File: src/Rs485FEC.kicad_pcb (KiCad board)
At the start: 2 copper layers, 24 x 27.9 mm, 21 parts, among them J1 B4B-XH-A, P1 105444-0001, Q1 DMP3099L-13, U1 FT232RL, U2 SP485E

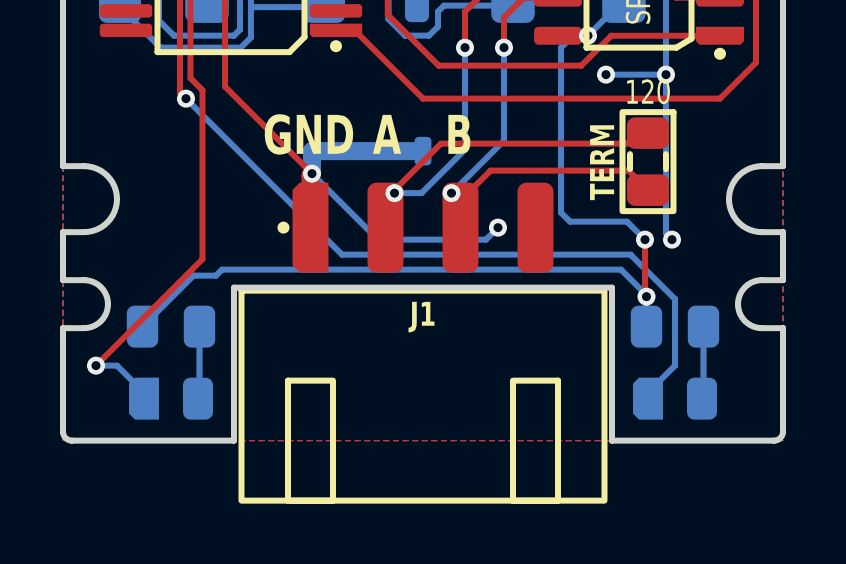
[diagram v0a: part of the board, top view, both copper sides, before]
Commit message: Updated connector designators
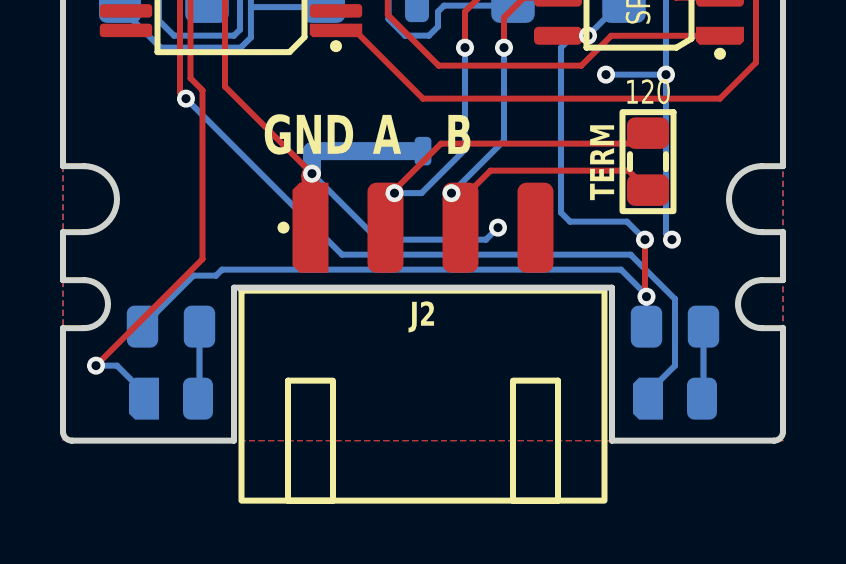
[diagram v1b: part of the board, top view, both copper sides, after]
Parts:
- renumbered P1 to J1, J1 to J2
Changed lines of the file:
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@@
     (descr "Molex 1054440001")
     (attr smd)
-    (fp_text reference "P1" (at 0 -1.7) (layer "F.SilkS") hide
+    (fp_text reference "J1" (at 0 -1.7) (layer "F.SilkS") hide
         (effects (font (size 0.8 0.6) (thickness 0.15)))
     )
@@
     (descr "JST B4B-XH-A [455-B4B-XH-A-ND]")
     (attr through_hole)
-    (fp_text reference "J1" (at 0 2.9) (layer "F.SilkS")
+    (fp_text reference "J2" (at 0 2.9) (layer "F.SilkS")
         (effects (font (size 0.8 0.6) (thickness 0.15) bold))
     )

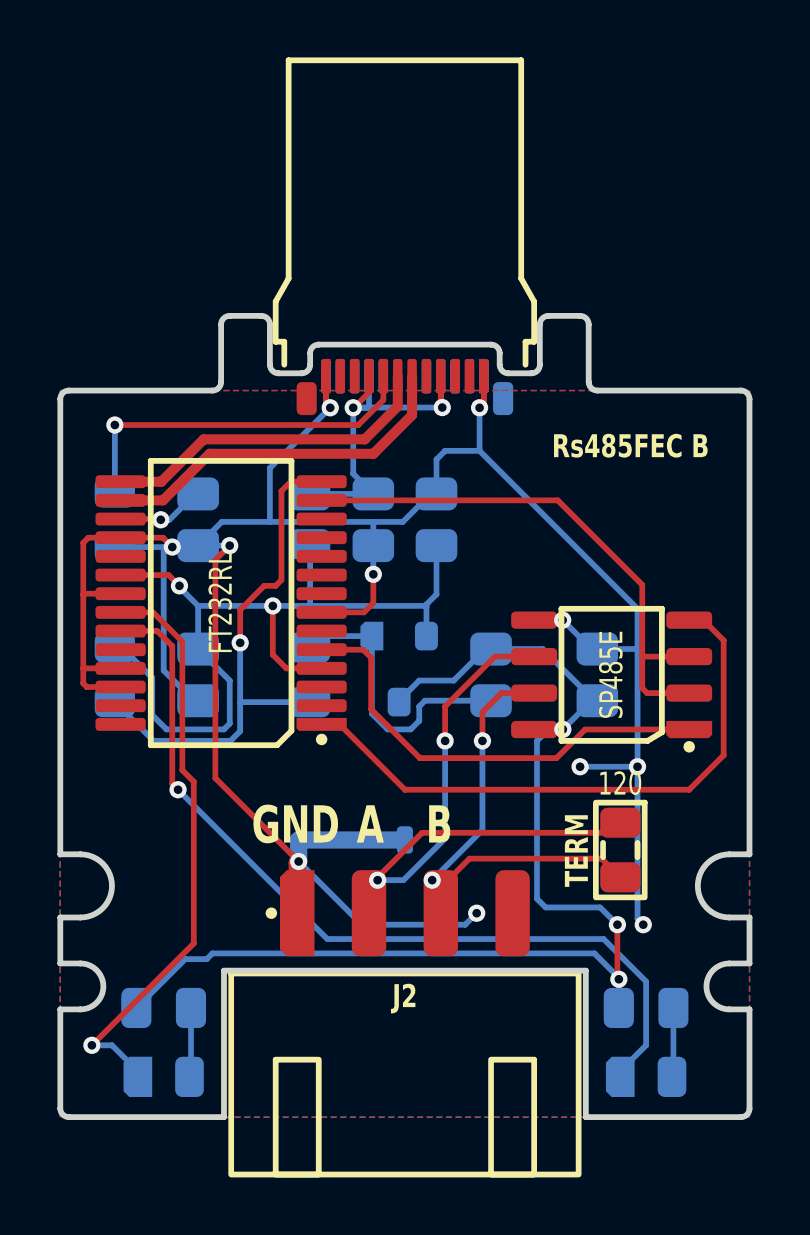
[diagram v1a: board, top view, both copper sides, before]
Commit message: Updated for KiCAD 8
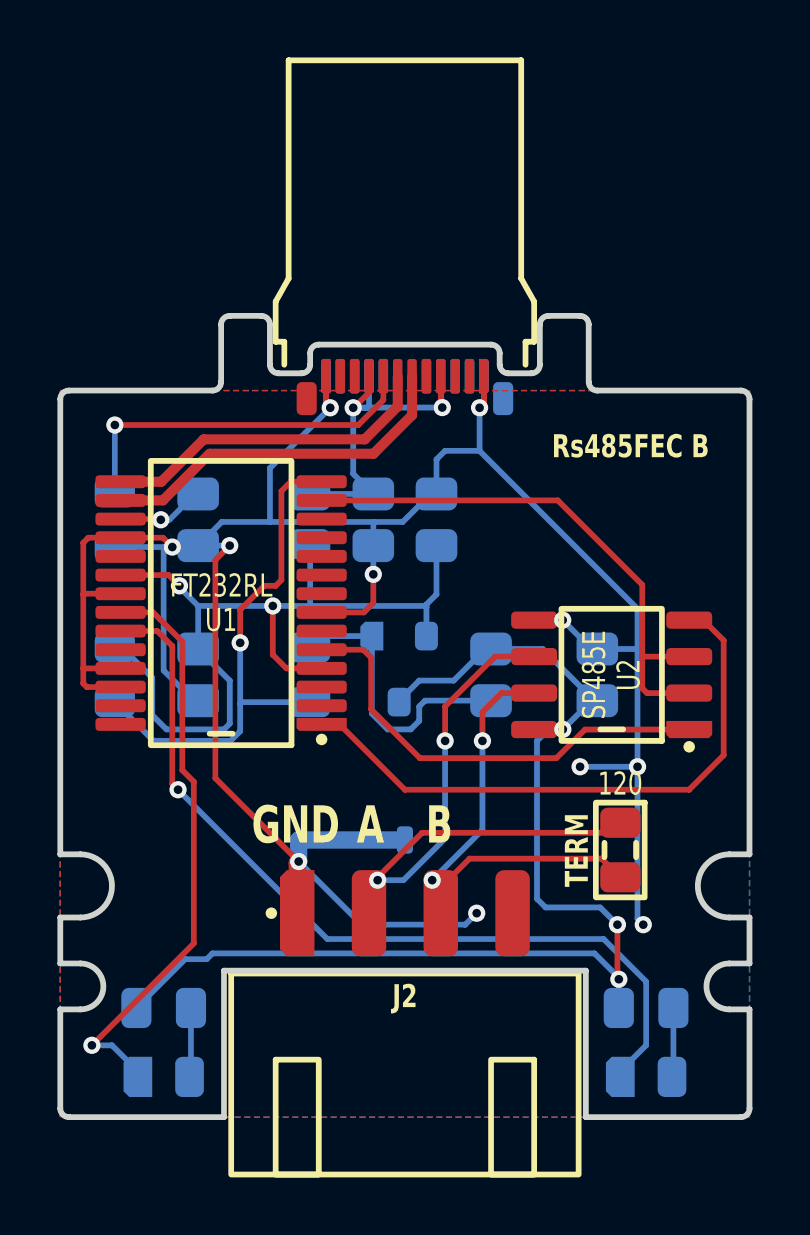
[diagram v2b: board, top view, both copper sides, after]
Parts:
- D1: footprint Medo64:D TVS SM05T1G (SOT23-3) -> Medo64:D TVS 7-12V [SM712] (SOT23-3)
- U1: footprint Medo64:U Transciever UART FT232RL (SSOP-28) -> Medo64:U Transceiver UART [FT232R] (SSOP-28)
- U2: footprint Medo64:U Transciever RS485 SP485E (SOIC-8) -> Medo64:U Transciever RS485 [SP485EEN] (SOIC-8)

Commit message: Added current limiting
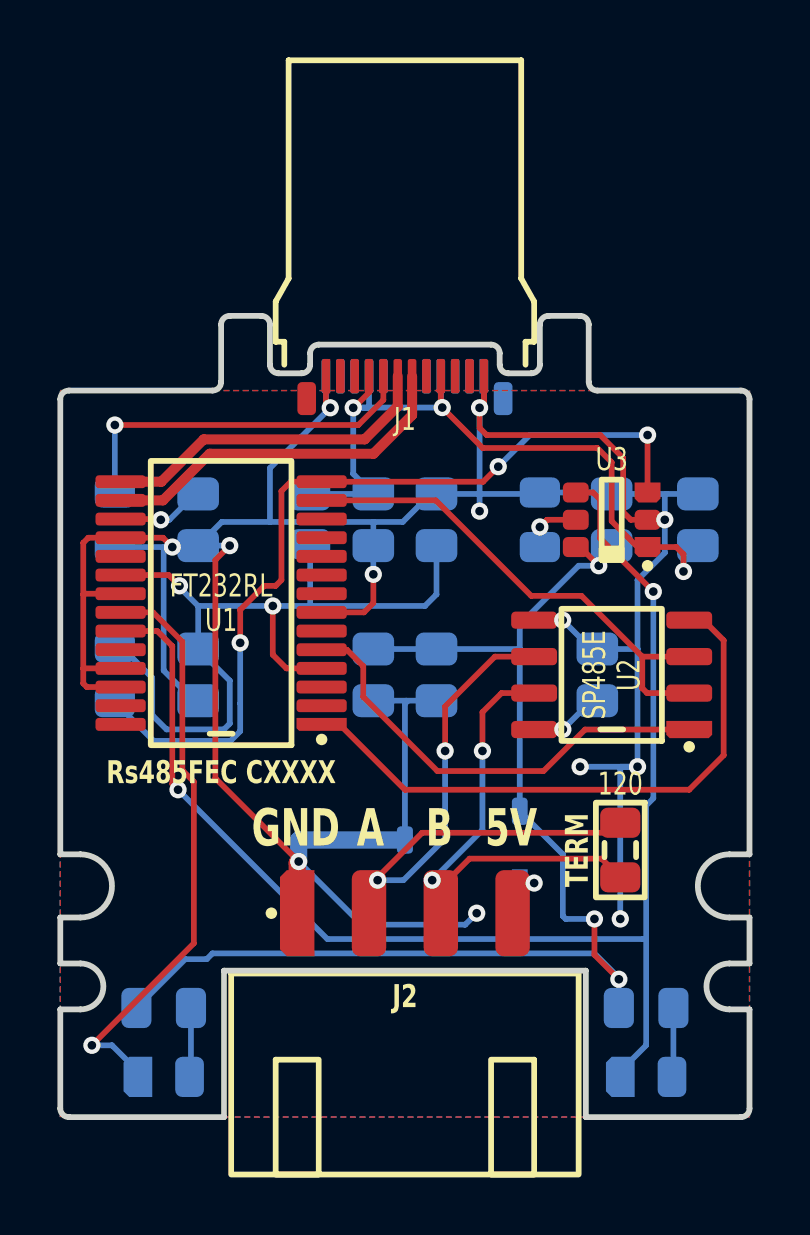
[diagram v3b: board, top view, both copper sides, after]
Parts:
- removed Q1: DMP3099L-13, Medo64:Q MOSFET-P (SOT23-3)
- removed R4: 1K, Medo64:R (0805)
- added C4: 100n, Medo64:C (0805), B.Cu at (42.2, 27.1)
- added C7: 10u, Medo64:C (0805), B.Cu at (30.9, 32.5)
- added C8: 10u, Medo64:C (0805), B.Cu at (33.1, 32.5)
- added D1: CUS08F30, Medo64:D (SOD323), B.Cu at (36.0, 38.5)
- added R6: 75K, Medo64:R (0805), B.Cu at (36.7, 27.1)
- added U3: AP22652, Medo64:U LoadSwitch Adjustable [AP22652W6-7] (SOT23-6), F.Cu at (39.2, 27.1)
- C6: renamed from C11; value 4u7 -> 10u
- J1: footprint Medo64:P USB C 3.2 Edge (24w) -> Medo64:J USB C 3.2 Edge (24w)
- moved C5 6.84 mm to (39.2, 27.1)
- renumbered D1 to D2, R6 to R5
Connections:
- net 3V3 renamed 3V3_UART_USB
- net USB_Vin renamed 5V_USB
- C4 pad 2: 5V_SW -> 5V_SWITCHED
- C5 pad 1: PWREN#' -> 5V_SWITCHED
- C5 pad 2: 5V_SW -> GND
- J2 pad 4: (no net) -> 5V_OUT
- R2 pad 1: 5V_SW -> 5V_SWITCHED
- R3 pad 1: 5V_SW -> 5V_SWITCHED
- U2 pad 8: 5V_SW -> 5V_SWITCHED
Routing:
- net 5V_SWITCHED: track 0.00 -> 47.1 mm, vias 0 -> 4
- net 5V_SW: track 40.9 -> 0.00 mm, vias 3 -> 0
- net GND: track 102.0 -> 123.4 mm, vias 11 -> 13
- net LED_TXD: track 29.7 -> 47.7 mm, vias 1 -> 2
- net 5V_USB: track 13.6 -> 26.4 mm, vias 2 -> 3
- net PWREN#: track 18.2 -> 29.8 mm, vias 1 -> 3
- net PWREN#': track 9.53 -> 0.00 mm
- net ILIMIT: track 0.00 -> 2.05 mm, vias 0 -> 1
- net TXDEN: track 19.3 -> 17.9 mm
- net 5V_OUT: track 0.00 -> 1.25 mm, vias 0 -> 1
- net 5V: track 30.5 -> 29.4 mm
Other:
- board text added: "5V"
- board text added: "Rs485FEC CXXXX"
- board text removed: "Rs485FEC B"

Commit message: Fixed refdes
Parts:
- renumbered C4 to C5, C5 to C6, C6 to C7, C7 to C8, C8 to C9
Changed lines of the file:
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@@
 		(at 33.1 32.5 -90)
 		(tags "CAPC2013X140N")
-		(property "Reference" "C8"
+		(property "Reference" "C9"
 			(at 0 1.6 90)
 			(layer "B.SilkS")
@@
 		(at 39.2 27.1 90)
 		(tags "CAPC2013X140N")
-		(property "Reference" "C5"
+		(property "Reference" "C6"
 			(at 0 1.6 90)
 			(layer "B.SilkS")
@@
 		(at 30.9 32.5 -90)
 		(tags "CAPC2013X140N")
-		(property "Reference" "C7"
+		(property "Reference" "C8"
 			(at 0 1.6 90)
 			(layer "B.SilkS")
@@
 		(at 42.2 27.1 90)
 		(tags "CAPC2013X140N")
-		(property "Reference" "C4"
+		(property "Reference" "C5"
 			(at 0 1.6 90)
 			(layer "B.SilkS")
@@
 		(at 33.1 27.1 -90)
 		(tags "CAPC2013X140N")
-		(property "Reference" "C6"
+		(property "Reference" "C7"
 			(at 0 1.6 90)
 			(layer "B.SilkS")
